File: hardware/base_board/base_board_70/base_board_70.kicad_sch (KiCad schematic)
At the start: 9 parts, among them IC1 single_pad, IC2 single_pad, J1 conn_2x2

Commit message: base_boards 60, 70 and 82
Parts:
- removed H1, H2: MountingHole, cycfi_library:hole_3mm, symbol Mechanical:MountingHole
- removed H5, H6: single_pad, xr_spectra_library:rail_slot_4.0, symbol cycfi_library:single_pad
- IC1, IC2, OC1, OC2: footprint cycfi_library:single-pad-1.6x1.6_circular -> Connector_PinHeader_2.54mm:PinHeader_1x01_P2.54mm_Vertical
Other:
- note removed: "Mounting Holes"
- company: (none) -> Document No. 2024006
- title: (none) -> XR Spectra Base Board 70
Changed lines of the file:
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@@
 (kicad_sch (version 20211123) (generator eeschema)
   (paper "A4")
-  (junction (at 167.64 97.79) (diameter 0) (color 0 0 0 0)
+  (title_block
+    (title "XR Spectra Base Board 70")
+    (date "2024-12-01")
+    (rev "v3.0")
+    (company "Document No. 2024006")
   )
   (junction (at 166.37 77.47) (diameter 0) (color 0 0 0 0)
@@
     (stroke (width 0) (type default) (color 0 0 0 0))
   )
-  (wire (pts (xy 170.18 97.79) (xy 167.64 97.79))
-    (stroke (width 0) (type default) (color 0 0 0 0))
-  )
   (wire (pts (xy 130.81 73.66) (xy 135.89 73.66))
     (stroke (width 0) (type default) (color 0 0 0 0))
@@
     (stroke (width 0) (type default) (color 0 0 0 0))
   )
-  (wire (pts (xy 167.64 104.14) (xy 167.64 97.79))
-    (stroke (width 0) (type default) (color 0 0 0 0))
-  )
   (wire (pts (xy 148.59 73.66) (xy 158.75 73.66))
     (stroke (width 0) (type default) (color 0 0 0 0))
@@
     (stroke (width 0) (type default) (color 0 0 0 0))
   )
-  (wire (pts (xy 162.56 97.79) (xy 162.56 100.33))
-    (stroke (width 0) (type default) (color 0 0 0 0))
-  )
-  (wire (pts (xy 170.18 104.14) (xy 167.64 104.14))
-    (stroke (width 0) (type default) (color 0 0 0 0))
-  )
   (polyline (pts (xy 152.4 101.6) (xy 123.19 101.6))
-    (stroke (width 0) (type default) (color 0 0 0 0))
-  )
-  (wire (pts (xy 167.64 97.79) (xy 162.56 97.79))
     (stroke (width 0) (type default) (color 0 0 0 0))
   )
@@
     (effects (font (size 1.27 1.27)) (justify left bottom))
   )
-  (text "Mounting Holes" (at 193.04 93.98 0)
-    (effects (font (size 1.27 1.27)) (justify left bottom))
-  )
   (text "June 17, 2021" (at 207.01 194.31 0)
     (effects (font (size 1.27 1.27)) (justify left bottom))
@@
       (effects (font (size 1.27 1.27)) hide)
     )
-    (property "Footprint" "cycfi_library:single-pad-1.6x1.6_circular" (id 2) (at 172.72 71.12 0)
+    (property "Footprint" "Connector_PinHeader_2.54mm:PinHeader_1x01_P2.54mm_Vertical" (id 2) (at 172.72 71.12 0)
       (effects (font (size 1.27 1.27)) hide)
     )
@@
       (effects (font (size 1.27 1.27)) hide)
     )
-    (property "Footprint" "cycfi_library:single-pad-1.6x1.6_circular" (id 2) (at 172.72 77.47 0)
+    (property "Footprint" "Connector_PinHeader_2.54mm:PinHeader_1x01_P2.54mm_Vertical" (id 2) (at 172.72 77.47 0)
       (effects (font (size 1.27 1.27)) hide)
     )
@@
     )
     (property "Datasheet" "~" (id 3) (at 130.81 74.93 0)
-      (effects (font (size 1.27 1.27)) hide)
-    )
-    (pin "1")
-  )
-  (symbol (lib_id "cycfi_library:single_pad") (at 172.72 97.79 270) (unit 1)
-    (in_bom yes) (on_board yes)
-    (property "Reference" "H5" (id 0) (at 175.895 97.79 0)
-      (effects (font (size 1.27 1.27)) (justify left) hide)
-    )
-    (property "Value" "single_pad" (id 1) (at 177.8 97.79 0)
-      (effects (font (size 1.27 1.27)) hide)
-    )
-    (property "Footprint" "xr_spectra_library:rail_slot_4.0" (id 2) (at 172.72 97.79 0)
-      (effects (font (size 1.27 1.27)) hide)
-    )
-    (property "Datasheet" "~" (id 3) (at 172.72 97.79 0)
-      (effects (font (size 1.27 1.27)) hide)
-    )
-    (pin "1")
-  )
-  (symbol (lib_id "power:GND") (at 162.56 100.33 0) (unit 1)
-    (in_bom yes) (on_board yes)
-    (property "Reference" "#PWR03" (id 0) (at 162.56 106.68 0)
-      (effects (font (size 1.27 1.27)) hide)
-    )
-    (property "Value" "GND" (id 1) (at 162.687 104.7242 0))
-    (property "Footprint" "" (id 2) (at 162.56 100.33 0)
-      (effects (font (size 1.27 1.27)) hide)
-    )
-    (property "Datasheet" "" (id 3) (at 162.56 100.33 0)
       (effects (font (size 1.27 1.27)) hide)
     )
@@
       (effects (font (size 1.27 1.27)) hide)
     )
-    (property "Footprint" "cycfi_library:single-pad-1.6x1.6_circular" (id 2) (at 172.72 90.17 0)
+    (property "Footprint" "Connector_PinHeader_2.54mm:PinHeader_1x01_P2.54mm_Vertical" (id 2) (at 172.72 90.17 0)
       (effects (font (size 1.27 1.27)) hide)
     )
@@
       (effects (font (size 1.27 1.27)) hide)
     )
-    (property "Footprint" "cycfi_library:single-pad-1.6x1.6_circular" (id 2) (at 172.72 83.82 0)
+    (property "Footprint" "Connector_PinHeader_2.54mm:PinHeader_1x01_P2.54mm_Vertical" (id 2) (at 172.72 83.82 0)
       (effects (font (size 1.27 1.27)) hide)
     )
     (property "Datasheet" "~" (id 3) (at 172.72 83.82 0)
-      (effects (font (size 1.27 1.27)) hide)
-    )
-    (pin "1")
-  )
-  (symbol (lib_id "cycfi_library:single_pad") (at 172.72 104.14 270) (unit 1)
-    (in_bom yes) (on_board yes)
-    (property "Reference" "H6" (id 0) (at 175.895 104.14 0)
-      (effects (font (size 1.27 1.27)) (justify left) hide)
-    )
-    (property "Value" "single_pad" (id 1) (at 177.8 104.14 0)
-      (effects (font (size 1.27 1.27)) hide)
-    )
-    (property "Footprint" "xr_spectra_library:rail_slot_4.0" (id 2) (at 172.72 104.14 0)
-      (effects (font (size 1.27 1.27)) hide)
-    )
-    (property "Datasheet" "~" (id 3) (at 172.72 104.14 0)
       (effects (font (size 1.27 1.27)) hide)
     )
@@
     )
     (pin "1")
-  )
-  (symbol (lib_id "Mechanical:MountingHole") (at 199.39 81.28 0) (unit 1)
-    (in_bom yes) (on_board yes) (fields_autoplaced)
-    (property "Reference" "H1" (id 0) (at 201.93 80.4453 0)
-      (effects (font (size 1.27 1.27)) (justify left))
-    )
-    (property "Value" "MountingHole" (id 1) (at 201.93 82.9822 0)
-      (effects (font (size 1.27 1.27)) (justify left) hide)
-    )
-    (property "Footprint" "cycfi_library:hole_3mm" (id 2) (at 199.39 81.28 0)
-      (effects (font (size 1.27 1.27)) hide)
-    )
-    (property "Datasheet" "~" (id 3) (at 199.39 81.28 0)
-      (effects (font (size 1.27 1.27)) hide)
-    )
   )
   (symbol (lib_id "Connector_Generic:Conn_02x02_Counter_Clockwise") (at 140.97 71.12 0) (unit 1)
@@
     (pin "4")
   )
-  (symbol (lib_id "Mechanical:MountingHole") (at 199.39 87.63 0) (unit 1)
-    (in_bom yes) (on_board yes) (fields_autoplaced)
-    (property "Reference" "H2" (id 0) (at 201.93 88.0638 0)
-      (effects (font (size 1.27 1.27)) (justify left))
-    )
-    (property "Value" "MountingHole" (id 1) (at 201.93 89.3322 0)
-      (effects (font (size 1.27 1.27)) (justify left) hide)
-    )
-    (property "Footprint" "cycfi_library:hole_3mm" (id 2) (at 199.39 87.63 0)
-      (effects (font (size 1.27 1.27)) hide)
-    )
-    (property "Datasheet" "~" (id 3) (at 199.39 87.63 0)
-      (effects (font (size 1.27 1.27)) hide)
-    )
-  )
   (sheet_instances
     (path "/" (page "1"))
@@
       (reference "#PWR01") (unit 1) (value "GND") (footprint "")
     )
-    (path "/00000000-0000-0000-0000-00006112c732"
-      (reference "#PWR03") (unit 1) (value "GND") (footprint "")
-    )
-    (path "/6f1beb86-67e1-46bf-8c2b-6d1e1485d5c0"
-      (reference "H1") (unit 1) (value "MountingHole") (footprint "cycfi_library:hole_3mm")
-    )
-    (path "/b90f2dfd-9639-4bac-9825-9f33089900c6"
-      (reference "H2") (unit 1) (value "MountingHole") (footprint "cycfi_library:hole_3mm")
-    )
-    (path "/00000000-0000-0000-0000-00006112bc09"
-      (reference "H5") (unit 1) (value "single_pad") (footprint "xr_spectra_library:rail_slot_4.0")
-    )
-    (path "/00000000-0000-0000-0000-00006114c19e"
-      (reference "H6") (unit 1) (value "single_pad") (footprint "xr_spectra_library:rail_slot_4.0")
-    )
     (path "/00000000-0000-0000-0000-000061122909"
-      (reference "IC1") (unit 1) (value "single_pad") (footprint "cycfi_library:single-pad-1.6x1.6_circular")
+      (reference "IC1") (unit 1) (value "single_pad") (footprint "Connector_PinHeader_2.54mm:PinHeader_1x01_P2.54mm_Vertical")
     )
     (path "/00000000-0000-0000-0000-00006112ffae"
-      (reference "IC2") (unit 1) (value "single_pad") (footprint "cycfi_library:single-pad-1.6x1.6_circular")
+      (reference "IC2") (unit 1) (value "single_pad") (footprint "Connector_PinHeader_2.54mm:PinHeader_1x01_P2.54mm_Vertical")
     )
     (path "/8d2043d0-1e2a-47a8-b40c-1d3c6b8242cf"
@@
     )
     (path "/00000000-0000-0000-0000-000061122fed"
-      (reference "OC1") (unit 1) (value "single_pad") (footprint "cycfi_library:single-pad-1.6x1.6_circular")
+      (reference "OC1") (unit 1) (value "single_pad") (footprint "Connector_PinHeader_2.54mm:PinHeader_1x01_P2.54mm_Vertical")
     )
     (path "/00000000-0000-0000-0000-0000611302a2"
-      (reference "OC2") (unit 1) (value "single_pad") (footprint "cycfi_library:single-pad-1.6x1.6_circular")
-    )
-  )
+      (reference "OC2") (unit 1) (value "single_pad") (footprint "Connector_PinHeader_2.54mm:PinHeader_1x01_P2.54mm_Vertical")
+    )
+  )

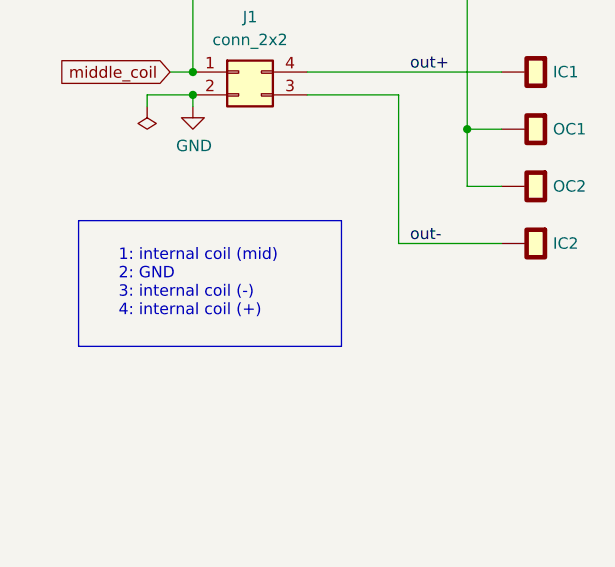
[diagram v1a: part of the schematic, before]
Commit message: Moved coil solder pads to outer perimeter
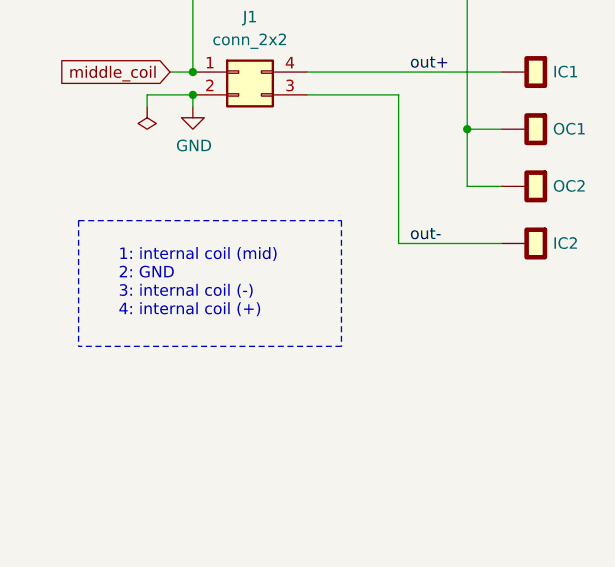
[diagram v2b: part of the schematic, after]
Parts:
- IC1, IC2, OC1, OC2: footprint Connector_PinHeader_2.54mm:PinHeader_1x01_P2.54mm_Vertical -> cycfi_library:xr_spectra_coil_pads

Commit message: Reversing the coil polarity
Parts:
- renumbered OC1 to IC1, OC2 to IC2, IC1 to OC1, IC2 to OC2
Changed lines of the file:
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@@
 		(on_board yes)
 		(dnp no)
-		(property "Reference" "IC1"
+		(property "Reference" "OC1"
 			(at 175.895 71.12 90)
 			(effects
@@
 			(project ""
 				(path "/b994142f-02ac-4881-9587-6d3df53c96d2"
-					(reference "IC1")
+					(reference "OC1")
 					(unit 1)
 				)
@@
 		(on_board yes)
 		(dnp no)
-		(property "Reference" "OC1"
+		(property "Reference" "IC1"
 			(at 175.895 77.47 90)
 			(effects
@@
 			(project ""
 				(path "/b994142f-02ac-4881-9587-6d3df53c96d2"
-					(reference "OC1")
+					(reference "IC1")
 					(unit 1)
 				)
@@
 		(on_board yes)
 		(dnp no)
-		(property "Reference" "IC2"
+		(property "Reference" "OC2"
 			(at 175.895 90.17 90)
 			(effects
@@
 			(project ""
 				(path "/b994142f-02ac-4881-9587-6d3df53c96d2"
-					(reference "IC2")
+					(reference "OC2")
 					(unit 1)
 				)
@@
 		(on_board yes)
 		(dnp no)
-		(property "Reference" "OC2"
+		(property "Reference" "IC2"
 			(at 175.895 83.82 90)
 			(effects
@@
 			(project ""
 				(path "/b994142f-02ac-4881-9587-6d3df53c96d2"
-					(reference "OC2")
-					(unit 1)
-				)
+					(reference "IC2")
+					(unit 1)
+				)
